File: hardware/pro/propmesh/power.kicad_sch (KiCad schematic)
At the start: 33 parts, among them J1 DC_IN, J2 DC_JACK, Q2 AOD4185, U1 TLV62569DBV, U2 AP64350SP-13

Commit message: Pro schematic complete; enclosure, layout guide, timeline and radio decisions
Schematic: all seven design sheets drawn and green; project-wide ERC at
zero. IR receiver dropped (hidden board can't see a remote — plug-in on
a DIGITAL_IN); GPIO 3 became LED_STRIP_1_CLK; both strip outputs 3- or
4-wire through one octal SN74AHCT541DWR (three revisions of the shifter
in one day, no mode jumpers). Input FET symbol replaced: KiCad 10's
Device:Q_PMOS numbers pins D/G/S and matches no pad — the part would
have been unconnected with no ERC/DRC complaint. All 196 references
renumbered to standard sequential designators (yaml keeps spec names;
the checker prints both). Sheet 08 (test points) and the sheet 01
staged-power link headers specified per spec §2.6 — sheet 01's checker
is red until they are drawn.

checknet.py: symbol pins ⊆ footprint pads check (the silent killer),
multi-unit pin keys + per-unit diagrams (`units:`), symbol-vote sheet
anchoring for half-drawn sheets, orientation-aware net voting, foreign
part reporting, cross-sheet extras no longer crash the report.

Docs: hardware/pro/layout.md — placement by designator, IPC-2221 trace
widths, thermal, silk, ⚠ list, KiCad primer; every chip's datasheet
layout section read (WROOM-1U has NO keep-out; DRV8871 wants a bottom
GND pour; MAX98357A output-trace numbers). Enclosure plan (spec §2.3):
Multilink RNI-1500 / RNI-300, DRiBOX Medium, Joinfworld clear-lid box,
icotek KEL-DPZ entry plate, fit rule 210×140×60 mm inside; PSU
defaults (§2.9) and the 10 A input-path note. Software plan: timeline
design (ramps native, live scrub v1, Cue.start_offset_ms in schema),
yard access (walk-up AP, WireGuard-in-firmware, BYO remote), WiFi-PHY
radio decision vs Zigbee/BLE/LoRa, console served-from-bridge budget,
USB stays in CDC/JTAG mode (no auto-program transistors needed).

Co-Authored-By: Claude Fable 5.1 <noreply@anthropic.com>
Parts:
- removed Q2: AOD4185, Package_TO_SOT_SMD:TO-252-2, symbol Device:Q_PMOS
- added Q7: AOD4185, Package_TO_SOT_SMD:TO-252-2, symbol Transistor_FET:SUD50P04-08
- renumbered C12 to C10, C2 to C12, C5 to C13, C6 to C14, C1 to C15, C7 to C16, C8 to C17, C3 to C6, C9 to C7, C4 to C8, C10 to C9, D3 to D10, D4 to D11, D1 to D8, D2 to D9, J1 to J17, J2 to J18, R9 to R13, R1 to R14, R2 to R15, R8 to R16, R5 to R17, R3 to R18, R4 to R19, R7 to R20, R6 to R21, U2 to U5, U1 to U6
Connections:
- net VIN_PROT: now also Q7.3 (S)
- net at D8.2 (A), R13.1: now also Q7.1 (G)
- net at F1.2: now also Q7.2 (D)

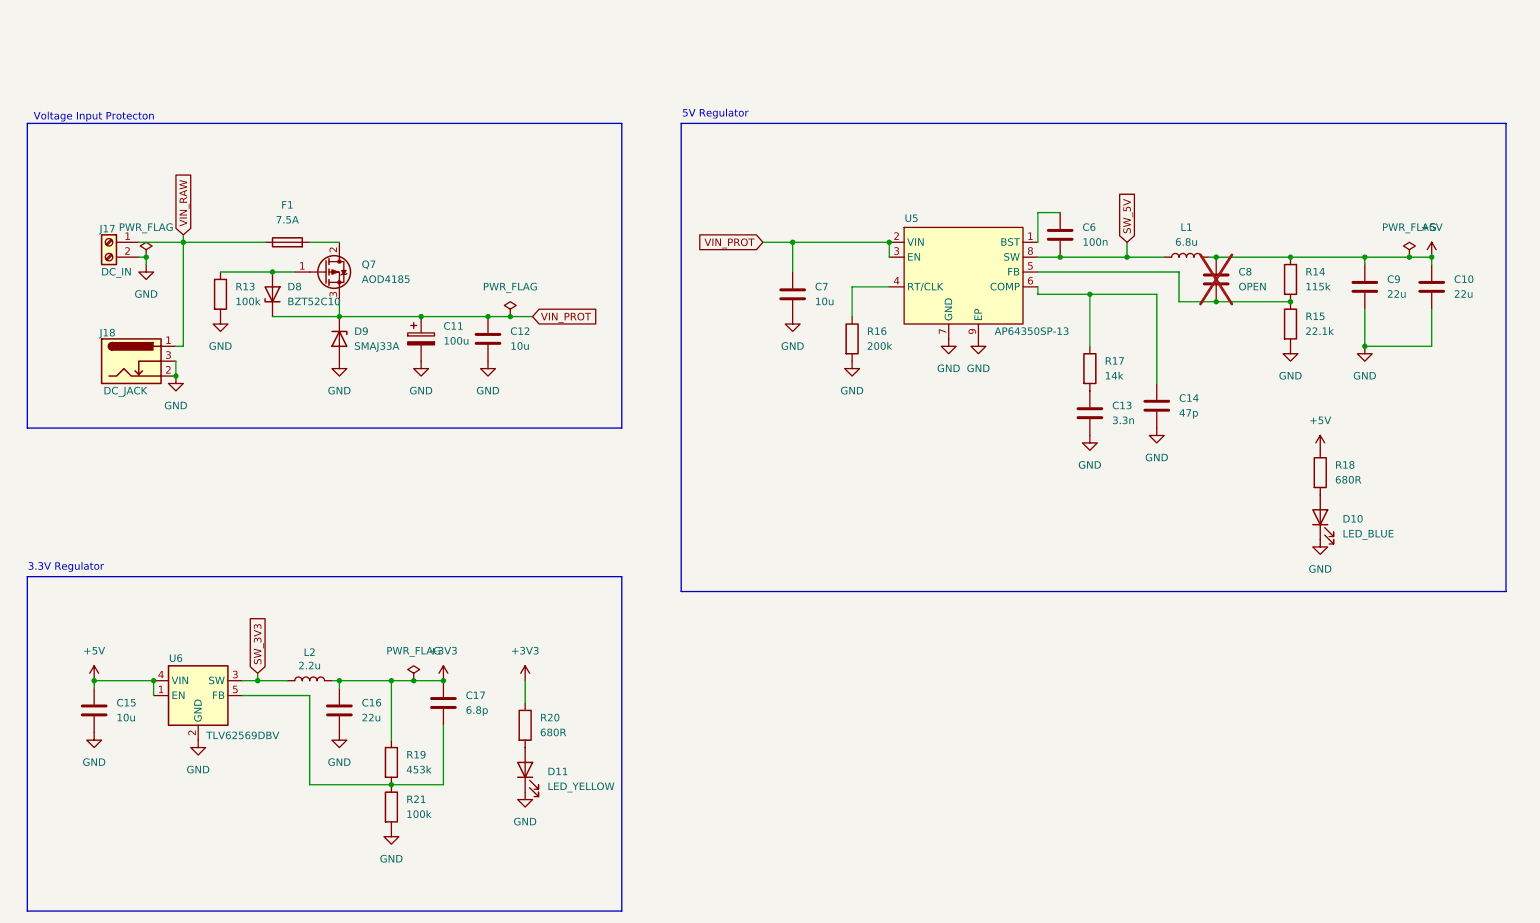
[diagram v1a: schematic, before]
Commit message: Sheet 08 (test points) + staged-power link headers; board synced 239/239
Sheet 08: 33 GPIO test points, 6 rail pads, DNP strap pad on GPIO 3 —
labels, values, wires and footprints generated from the yaml
(tools-side, not typed), power symbols cloned with every coordinate
shifted so texts travel with their parts. Sheet 01: JP_VIN / JP_5V /
JP_3V3 2-pin headers + shunts between input → 5 V buck → +5V rail →
+3V3 rail (spec §2.6 staged bring-up; a meter across a pulled shunt
reads that rail's current); PWR_FLAGs re-homed to the far side of each
jumper. Values use Colin's JP_* names; jumper pin numbering follows
the drawing.

All eight sheets green, ERC 0 violations, board updated with orphan
deletion: 239 footprints for 239 symbols, none differing.

checknet.py: extras from other sheets no longer crash the report or
the diagram renderer.

Co-Authored-By: Claude Fable 5.1 <noreply@anthropic.com>
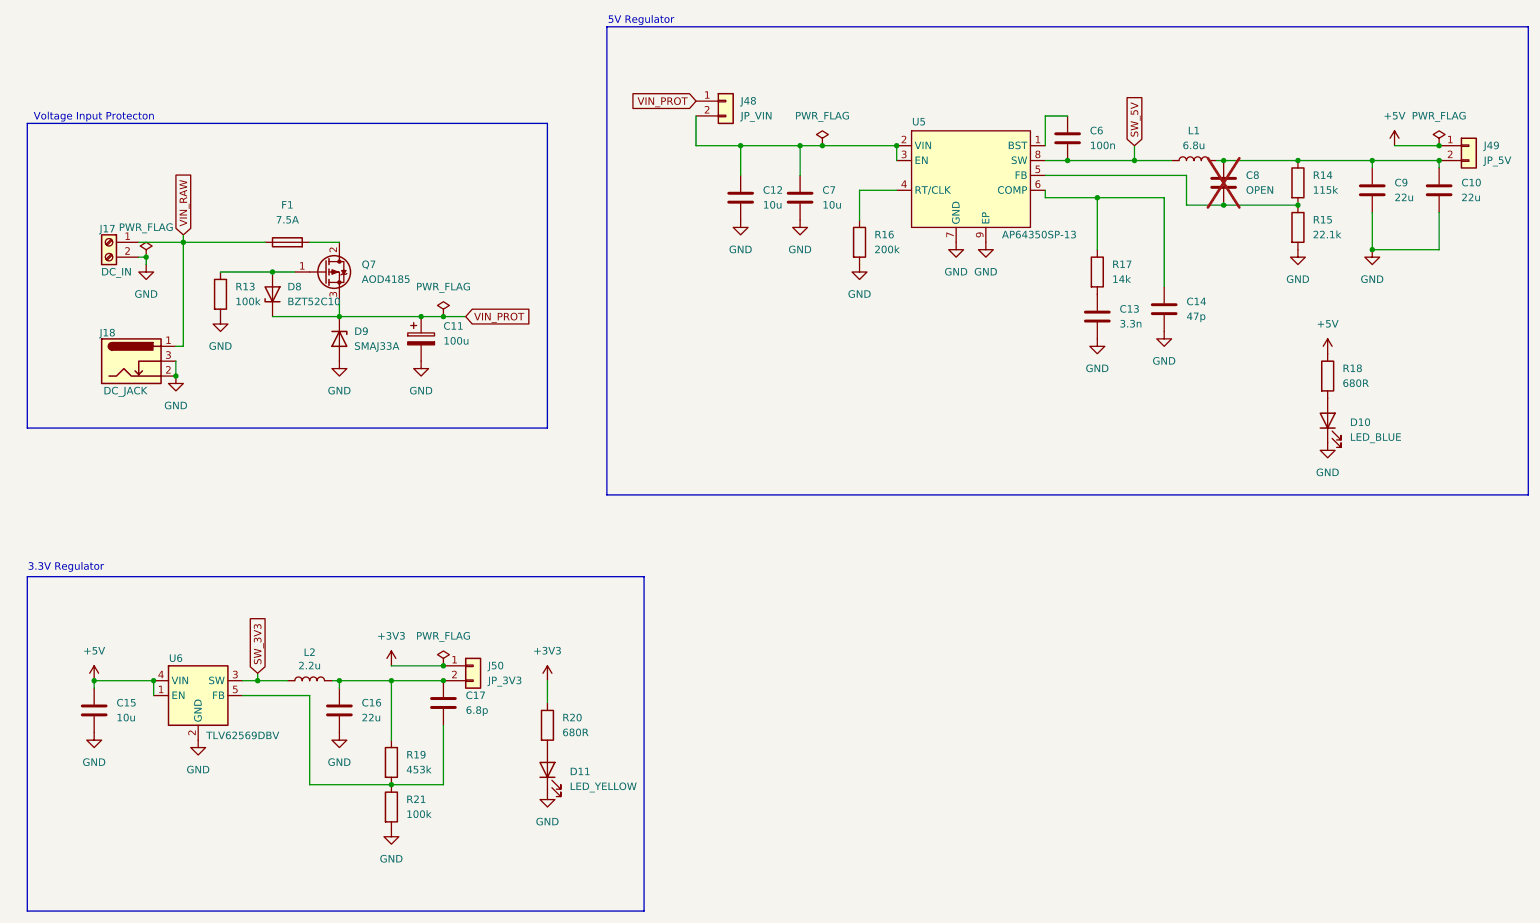
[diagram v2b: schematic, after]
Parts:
- added J48: JP_VIN, Connector_PinHeader_2.54mm:PinHeader_1x02_P2.54mm_Vertical, symbol Connector_Generic:Conn_01x02
- added J49: JP_5V, Connector_PinHeader_2.54mm:PinHeader_1x02_P2.54mm_Vertical, symbol Connector_Generic:Conn_01x02
- added J50: JP_3V3, Connector_PinHeader_2.54mm:PinHeader_1x02_P2.54mm_Vertical, symbol Connector_Generic:Conn_01x02
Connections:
- net +3V3: now also J50.1 (Pin_1); no longer C16.1, C17.1, L2.2, R19.1
- net +5V: now also J49.1 (Pin_1); no longer C10.1, C8.1, C9.1, L1.2, R14.1
- net VIN_PROT: now also J48.1 (Pin_1); no longer C12.1, C7.1, U5.2 (VIN), U5.3 (EN)
- new net: C16.1, C17.1, J50.2 (Pin_2), L2.2, R19.1
- new net: C10.1, C8.1, C9.1, J49.2 (Pin_2), L1.2, R14.1
- new net: C12.1, C7.1, J48.2 (Pin_2), U5.2 (VIN), U5.3 (EN)
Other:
- moved on the sheet: C10, C12, C13, C14, C6, C7, C8, C9, D10, D11, L1, R14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

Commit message: Pro v0.1: board setup + placement, two design reviews applied, datasheet-review changes specced
Checkpoint of two weeks' work since dacce25. The schematic is MID-EDIT:
sheets 02/04/05/07/08 checkers are red by design until the changes in
hardware/pro/schematic-changes-2026-09-16.md are drawn; sheet 03 is
half-drawn (see finish-v0.1.md).

Layout
- layout.md rebuilt as one ordered procedure (Part A) with a
  where-you-are line; Board Setup, outline, origin, frozen 120x90 hole
  pattern; routing and pour guidance; per-net noise keep-outs
- tools: checksetup.py (setup/outline/holes/netclasses/socket rows),
  placeboard.py, placetps.py (test points on B.Cu for bodge + pogo rig),
  setpos.py, snapgrid.py; placement renders; power/MCU placement tables

Reviews
- review-2026-09-08 (external audit): C1 EN cap, MA/MB_ILIM short,
  servo/output channel order, sensor clamp order, VIN_FUSED label,
  F1 footprint — all fixed in the schematic
- checknet.py: merged-net assertion (distinct spec nets must be
  distinct schematic nets) — the class that hid the ILIM short
- review-2026-09-16 (routing) + datasheet-review-2026-09-16 with a
  verified disposition; Mini plan audit + recommendations (other session)

Decisions 2026-09-16 (specs, pinmap and headers updated; drawing pending)
- 5 V rail: strip bulk 1000 uF -> 220 uF Rubycon C88757; JP_USB link
  makes USB power opt-in (AP64350 hiccups into 2 mF)
- sensor series R 1 k 0603 -> 2.2 k 1206 C17948 (24 V miswire)
- second PCA9685 (0x41, 1 kHz) for the six DC channels; servos stay at
  50 Hz on 0x40; both OE on GPIO 37 = PCA_OE with pull-up (pinmap:
  36/36 GPIO used; genpins.py supports several PCA9685s)
- output FETs Q1-Q6 -> 40 V Vishay SI2356DS C74127 (TVS coordination)
- SD DAT1/DAT2 pull-ups; USB 22R pair + DNP caps + VBUS 100 nF;
  74AHCT541 input pulldowns, R53 fitted
- MP6603 dual-mode socket mapping verified; MS strap defaults decided

Co-Authored-By: Claude Opus 5 (1M context) <noreply@anthropic.com>
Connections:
- net 3V3_BUCK: now reaches C16.1, C17.1, J50.2 (Pin_2), L2.2, R19.1
- net 5V_BUCK: now reaches C10.1, C8.1, C9.1, J49.2 (Pin_2), L1.2, R14.1
- net VIN_BUCK: now reaches C12.1, C7.1, J48.2 (Pin_2), U5.2 (VIN), U5.3 (EN)
- net VIN_FUSED: now reaches F1.2, Q7.2 (D)
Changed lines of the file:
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@@
-	(wire
-		(pts
-			(xy 156.21 50.8) (xy 168.91 50.8)
-		)
-		(stroke
-			(width 0)
-			(type default)
-		)
-	)
 	(wire
 		(pts
@@
 	(wire
 		(pts
-			(xy 142.24 50.8) (xy 152.4 50.8)
+			(xy 142.24 50.8) (xy 168.91 50.8)
 		)
 		(stroke
@@
 	(wire
 		(pts
-			(xy 152.4 50.8) (xy 156.21 50.8)
-		)
-		(stroke
-			(width 0)
-			(type default)
-		)
-	)
-	(wire
-		(pts
 			(xy 194.31 59.69) (xy 214.63 59.69)
 		)
@@
 		)
 	)
+	(label "VIN_FUSED"
+		(at 68.58 67.31 0)
+		(effects
+			(font
+				(size 1.27 1.27)
+			)
+			(justify left bottom)
+		)
+	)
+	(label "3V3_BUCK"
+		(at 74.93 142.24 0)
+		(effects
+			(font
+				(size 1.27 1.27)
+			)
+			(justify left bottom)
+		)
+	)
+	(label "5V_BUCK"
+		(at 232.41 53.34 0)
+		(effects
+			(font
+				(size 1.27 1.27)
+			)
+			(justify left bottom)
+		)
+	)
+	(label "VIN_BUCK"
+		(at 158.75 50.8 0)
+		(effects
+			(font
+				(size 1.27 1.27)
+			)
+			(justify left bottom)
+		)
+	)
